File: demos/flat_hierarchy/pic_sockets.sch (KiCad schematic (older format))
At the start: 8 parts, among them P2 SUPP28, P3 SUPP40, U1 24Cxx, U5 PIC_18_PINS, U6 PIC_8_PINS

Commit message: Update demo files
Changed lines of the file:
@@
 EESchema Schematic File Version 2
-LIBS:power,device,transistors,conn,linear,regul,74xx,cmos4000,adc-dac,memory,xilinx,special,microcontrollers,dsp,microchip,analog_switches,motorola,texas,intel,audio,interface,digital-audio,philips,display,cypress,siliconi,contrib,valves
-EELAYER 23  0
+LIBS:power
+LIBS:device
+LIBS:transistors
+LIBS:conn
+LIBS:linear
+LIBS:regul
+LIBS:74xx
+LIBS:cmos4000
+LIBS:adc-dac
+LIBS:memory
+LIBS:xilinx
+LIBS:special
+LIBS:microcontrollers
+LIBS:dsp
+LIBS:microchip
+LIBS:analog_switches
+LIBS:motorola
+LIBS:texas
+LIBS:intel
+LIBS:audio
+LIBS:interface
+LIBS:digital-audio
+LIBS:philips
+LIBS:display
+LIBS:cypress
+LIBS:siliconi
+LIBS:opto
+LIBS:atmel
+LIBS:flat_hierarchy-cache
+EELAYER 24 0
 EELAYER END
-$Descr A4 11700 8267
+$Descr A4 11693 8268
+encoding utf-8
 Sheet 2 3
 Title "JDM - COM84 PIC Programmer with 13V DC/DC converter"
@@
 Comment4 ""
 $EndDescr
-Text GLabel 2350 1900 0    60   Input
+Text GLabel 2350 1900 0    60   Input ~ 0
 VPP-MCLR
-Text GLabel 2350 1700 0    60   Input
-CLOCK-RB6
-Text GLabel 2350 1500 0    60   Input
-DATA-RB7
-Text GLabel 2350 2150 0    60   Input
-VCC_PIC
-Text Label 2550 2150 0    60   ~
-VCC_PIC
-Text Label 2450 3150 0    60   ~
+Text GLabel 2350 1700 0    60   Input ~ 0
+CLOCK-RB6
+Text GLabel 2350 1500 0    60   Input ~ 0
+DATA-RB7
+Text GLabel 2350 2150 0    60   Input ~ 0
+VCC_PIC
+Text Label 2550 2150 0    60   ~ 0
+VCC_PIC
+Text Label 2450 3150 0    60   ~ 0
 VPP-MCLR
 Wire Wire Line
@@
 Wire Wire Line
 	4550 6900 4550 7000
-Text Label 3950 6900 0    60   ~
+Text Label 3950 6900 0    60   ~ 0
 VCC_PIC
 $Comp
@@
 U 1 1 4639BE2E
 P 4550 7400
-F 0 "#PWR01" H 4550 7400 30  0001 C C
-F 1 "GND" H 4550 7330 30  0001 C C
+F 0 "#PWR01" H 4550 7400 30  0001 C CNN
+F 1 "GND" H 4550 7330 30  0001 C CNN
+F 2 "" H 4550 7400 60  0001 C CNN
+F 3 "" H 4550 7400 60  0001 C CNN
 	1    4550 7400
 	1    0    0    -1
@@
 U 1 1 4639BE2C
 P 4550 7200
-F 0 "C8" H 4600 7300 50  0000 L C
-F 1 "100nF" H 4600 7100 50  0000 L C
+F 0 "C8" H 4600 7300 50  0000 L CNN
+F 1 "100nF" H 4600 7100 50  0000 L CNN
+F 2 "" H 4550 7200 60  0001 C CNN
+F 3 "" H 4550 7200 60  0001 C CNN
 	1    4550 7200
 	1    0    0    -1
 $EndComp
-Text Label 7650 5150 0    60   ~
-VCC_PIC
-Text Label 9900 4950 0    60   ~
-VCC_PIC
-Text Label 9650 2500 0    60   ~
+Text Label 7650 5150 0    60   ~ 0
+VCC_PIC
+Text Label 9900 4950 0    60   ~ 0
+VCC_PIC
+Text Label 9650 2500 0    60   ~ 0
 VCC_PIC
 $Comp
@@
 U 1 1 442A8794
 P 8450 5250
-F 0 "#PWR02" H 8450 5250 30  0001 C C
-F 1 "GND" H 8450 5180 30  0001 C C
+F 0 "#PWR02" H 8450 5250 30  0001 C CNN
+F 1 "GND" H 8450 5180 30  0001 C CNN
+F 2 "" H 8450 5250 60  0001 C CNN
+F 3 "" H 8450 5250 60  0001 C CNN
 	1    8450 5250
 	0    1    1    0
 $EndComp
-Text Label 4300 4850 0    60   ~
+Text Label 4300 4850 0    60   ~ 0
 VCC_PIC
 $Comp
@@
 U 1 1 443CCA5D
 P 8450 4850
-F 0 "#PWR03" H 8450 4850 30  0001 C C
-F 1 "GND" H 8450 4780 30  0001 C C
+F 0 "#PWR03" H 8450 4850 30  0001 C CNN
+F 1 "GND" H 8450 4780 30  0001 C CNN
+F 2 "" H 8450 4850 60  0001 C CNN
+F 3 "" H 8450 4850 60  0001 C CNN
 	1    8450 4850
 	0    1    1    0
@@
 U 1 1 443697C7
 P 9400 2600
-F 0 "#PWR04" H 9400 2600 30  0001 C C
-F 1 "GND" H 9400 2530 30  0001 C C
+F 0 "#PWR04" H 9400 2600 30  0001 C CNN
+F 1 "GND" H 9400 2530 30  0001 C CNN
+F 2 "" H 9400 2600 60  0001 C CNN
+F 3 "" H 9400 2600 60  0001 C CNN
 	1    9400 2600
 	0    -1   -1   0
@@
 U 1 1 443697C3
 P 8200 2400
-F 0 "#PWR05" H 8200 2400 30  0001 C C
-F 1 "GND" H 8200 2330 30  0001 C C
+F 0 "#PWR05" H 8200 2400 30  0001 C CNN
+F 1 "GND" H 8200 2330 30  0001 C CNN
+F 2 "" H 8200 2400 60  0001 C CNN
+F 3 "" H 8200 2400 60  0001 C CNN
 	1    8200 2400
 	0    1    1    0
 $EndComp
-Text Label 9550 1800 0    60   ~
-CLOCK-RB6
-Text Label 9550 1700 0    60   ~
-DATA-RB7
-Text Label 7550 1700 0    60   ~
+Text Label 9550 1800 0    60   ~ 0
+CLOCK-RB6
+Text Label 9550 1700 0    60   ~ 0
+DATA-RB7
+Text Label 7550 1700 0    60   ~ 0
 VPP-MCLR
 $Comp
@@
 U 1 1 4436967E
 P 8800 2350
-F 0 "P2" H 8850 3150 70  0000 C C
-F 1 "SUPP28" H 8800 1550 70  0000 C C
+F 0 "P2" H 8850 3150 70  0000 C CNN
+F 1 "SUPP28" H 8800 1550 70  0000 C CNN
+F 2 "" H 8800 2350 60  0001 C CNN
+F 3 "" H 8800 2350 60  0001 C CNN
 	1    8800 2350
 	1    0    0    -1
@@
 U 1 1 442AA147
 P 3700 7400
-F 0 "#PWR06" H 3700 7400 30  0001 C C
-F 1 "GND" H 3700 7330 30  0001 C C
+F 0 "#PWR06" H 3700 7400 30  0001 C CNN
+F 1 "GND" H 3700 7330 30  0001 C CNN
+F 2 "" H 3700 7400 60  0001 C CNN
+F 3 "" H 3700 7400 60  0001 C CNN
 	1    3700 7400
 	1    0    0    -1
@@
 U 1 1 442AA145
 P 3700 7200
-F 0 "C7" H 3750 7300 50  0000 L C
-F 1 "100nF" H 3750 7100 50  0000 L C
+F 0 "C7" H 3750 7300 50  0000 L CNN
+F 1 "100nF" H 3750 7100 50  0000 L CNN
+F 2 "" H 3700 7200 60  0001 C CNN
+F 3 "" H 3700 7200 60  0001 C CNN
 	1    3700 7200
 	1    0    0    -1
@@
 U 1 1 442AA138
 P 2700 7400
-F 0 "#PWR07" H 2700 7400 30  0001 C C
-F 1 "GND" H 2700 7330 30  0001 C C
+F 0 "#PWR07" H 2700 7400 30  0001 C CNN
+F 1 "GND" H 2700 7330 30  0001 C CNN
+F 2 "" H 2700 7400 60  0001 C CNN
+F 3 "" H 2700 7400 60  0001 C CNN
 	1    2700 7400
 	1    0    0    -1
@@
 U 1 1 442AA134
 P 2700 7000
-F 0 "#PWR08" H 2700 7100 30  0001 C C
-F 1 "VCC" H 2700 7100 30  0000 C C
+F 0 "#PWR08" H 2700 7100 30  0001 C CNN
+F 1 "VCC" H 2700 7100 30  0000 C CNN
+F 2 "" H 2700 7000 60  0001 C CNN
+F 3 "" H 2700 7000 60  0001 C CNN
 	1    2700 7000
 	1    0    0    -1
@@
 U 1 1 442AA12B
 P 2700 7200
-F 0 "C6" H 2750 7300 50  0000 L C
-F 1 "100nF" H 2750 7100 50  0000 L C
+F 0 "C6" H 2750 7300 50  0000 L CNN
+F 1 "100nF" H 2750 7100 50  0000 L CNN
+F 2 "" H 2700 7200 60  0001 C CNN
+F 3 "" H 2700 7200 60  0001 C CNN
 	1    2700 7200
 	1    0    0    -1
@@
 U 1 1 442A896A
 P 9650 5050
-F 0 "#PWR09" H 9650 5050 30  0001 C C
-F 1 "GND" H 9650 4980 30  0001 C C
+F 0 "#PWR09" H 9650 5050 30  0001 C CNN
+F 1 "GND" H 9650 4980 30  0001 C CNN
+F 2 "" H 9650 5050 60  0001 C CNN
+F 3 "" H 9650 5050 60  0001 C CNN
 	1    9650 5050
 	0    -1   -1   0
@@
 U 1 1 442A88ED
 P 9050 5100
-F 0 "P3" H 9100 6200 70  0000 C C
-F 1 "SUPP40" H 8900 4000 70  0000 C C
+F 0 "P3" H 9100 6200 70  0000 C CNN
+F 1 "SUPP40" H 8900 4000 70  0000 C CNN
+F 2 "" H 9050 5100 60  0001 C CNN
+F 3 "" H 9050 5100 60  0001 C CNN
 	1    9050 5100
 	1    0    0    -1
@@
 U 1 1 442A8838
 P 2950 1250
-F 0 "#PWR010" H 2950 1250 30  0001 C C
-F 1 "GND" H 2950 1180 30  0001 C C
+F 0 "#PWR010" H 2950 1250 30  0001 C CNN
+F 1 "GND" H 2950 1180 30  0001 C CNN
+F 2 "" H 2950 1250 60  0001 C CNN
+F 3 "" H 2950 1250 60  0001 C CNN
 	1    2950 1250
 	1    0    0    -1
 $EndComp
-Text Label 4700 1400 0    60   ~
-DATA-RB7
-Text Label 4700 1300 0    60   ~
+Text Label 4700 1400 0    60   ~ 0
+DATA-RB7
+Text Label 4700 1300 0    60   ~ 0
 CLOCK-RB6
 $Comp
@@
 U 1 1 442A87F7
 P 3850 1200
-F 0 "U1" H 4000 1550 60  0000 C C
-F 1 "24Cxx" H 4050 850 60  0000 C C
+F 0 "U1" H 4000 1550 60  0000 C CNN
+F 1 "24Cxx" H 4050 850 60  0000 C CNN
+F 2 "" H 3850 1200 60  0001 C CNN
+F 3 "" H 3850 1200 60  0001 C CNN
 	1    3850 1200
 	1    0    0    -1
 $EndComp
-Text Label 9800 4250 0    60   ~
-CLOCK-RB6
-Text Label 9800 4150 0    60   ~
-DATA-RB7
-Text Label 7800 4150 0    60   ~
+Text Label 9800 4250 0    60   ~ 0
+CLOCK-RB6
+Text Label 9800 4150 0    60   ~ 0
+DATA-RB7
+Text Label 7800 4150 0    60   ~ 0
 VPP-MCLR
 NoConn ~ 2500 4400
@@
 U 1 1 442A81A7
 P 3300 4850
-F 0 "U5" H 3600 5650 60  0000 C C
-F 1 "PIC_18_PINS" H 3750 4050 60  0000 C C
+F 0 "U5" H 3600 5650 60  0000 C CNN
+F 1 "PIC_18_PINS" H 3750 4050 60  0000 C CNN
+F 2 "" H 3300 4850 60  0001 C CNN
+F 3 "" H 3300 4850 60  0001 C CNN
 	1    3300 4850
 	1    0    0    -1
@@
 NoConn ~ 3100 2850
 NoConn ~ 3100 2450
-Text Label 4200 5150 0    60   ~
-CLOCK-RB6
-Text Label 4200 5000 0    60   ~
-DATA-RB7
-Text Label 1850 4700 0    60   ~
+Text Label 4200 5150 0    60   ~ 0
+CLOCK-RB6
+Text Label 4200 5000 0    60   ~ 0
+DATA-RB7
+Text Label 1850 4700 0    60   ~ 0
 VPP-MCLR
-Text Label 4700 2850 0    60   ~
-CLOCK-RB6
-Text Label 4700 2450 0    60   ~
+Text Label 4700 2850 0    60   ~ 0
+CLOCK-RB6
+Text Label 4700 2450 0    60   ~ 0
 DATA-RB7
 $Comp
@@
 U 1 1 442A820F
 P 2300 4900
-F 0 "#PWR011" H 2300 4900 30  0001 C C
-F 1 "GND" H 2300 4830 30  0001 C C
+F 0 "#PWR011" H 2300 4900 30  0001 C CNN
+F 1 "GND" H 2300 4830 30  0001 C CNN
+F 2 "" H 2300 4900 60  0001 C CNN
+F 3 "" H 2300 4900 60  0001 C CNN
 	1    2300 4900
 	1    0    0    -1
@@
 U 1 1 442A8205
 P 4550 2150
-F 0 "#PWR012" H 4550 2150 30  0001 C C
-F 1 "GND" H 4550 2080 30  0001 C C
+F 0 "#PWR012" H 4550 2150 30  0001 C CNN
+F 1 "GND" H 4550 2080 30  0001 C CNN
+F 2 "" H 4550 2150 60  0001 C CNN
+F 3 "" H 4550 2150 60  0001 C CNN
 	1    4550 2150
 	0    -1   -1   0
@@
 U 1 1 442A81A5
 P 3850 2650
-F 0 "U6" H 3800 3350 60  0000 C C
-F 1 "PIC_8_PINS" H 3850 1950 60  0000 C C
+F 0 "U6" H 3800 3350 60  0000 C CNN
+F 1 "PIC_8_PINS" H 3850 1950 60  0000 C CNN
+F 2 "" H 3850 2650 60  0001 C CNN
+F 3 "" H 3850 2650 60  0001 C CNN
 	1    3850 2650
 	1    0    0    -1
 $EndComp
+$Comp
+L VCC #PWR013
+U 1 1 53B84749
+P 3850 700
+F 0 "#PWR013" H 3850 800 30  0001 C CNN
+F 1 "VCC" H 3850 800 30  0000 C CNN
+F 2 "" H 3850 700 60  0001 C CNN
+F 3 "" H 3850 700 60  0001 C CNN
+	1    3850 700
+	1    0    0    -1
+$EndComp
+$Comp
+L GND #PWR014
+U 1 1 53B847AC
+P 3850 1700
+F 0 "#PWR014" H 3850 1700 30  0001 C CNN
+F 1 "GND" H 3850 1630 30  0001 C CNN
+F 2 "" H 3850 1700 60  0001 C CNN
+F 3 "" H 3850 1700 60  0001 C CNN
+	1    3850 1700
+	1    0    0    -1
+$EndComp

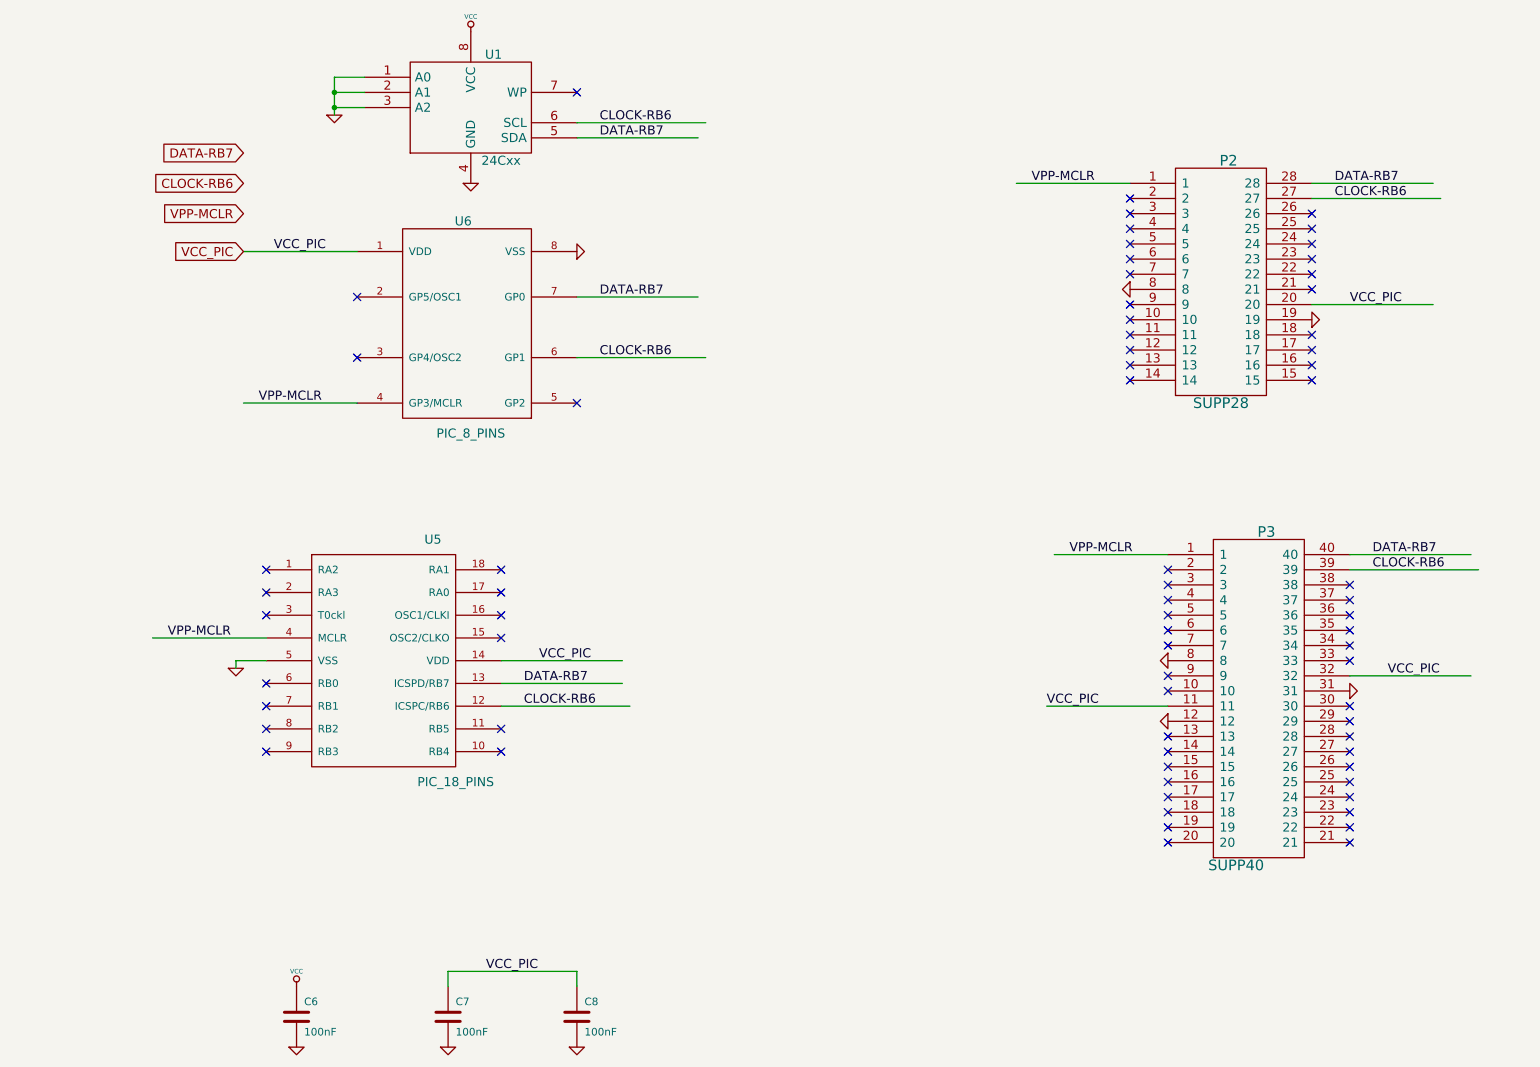
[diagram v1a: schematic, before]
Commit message: demos/ schematic tidying
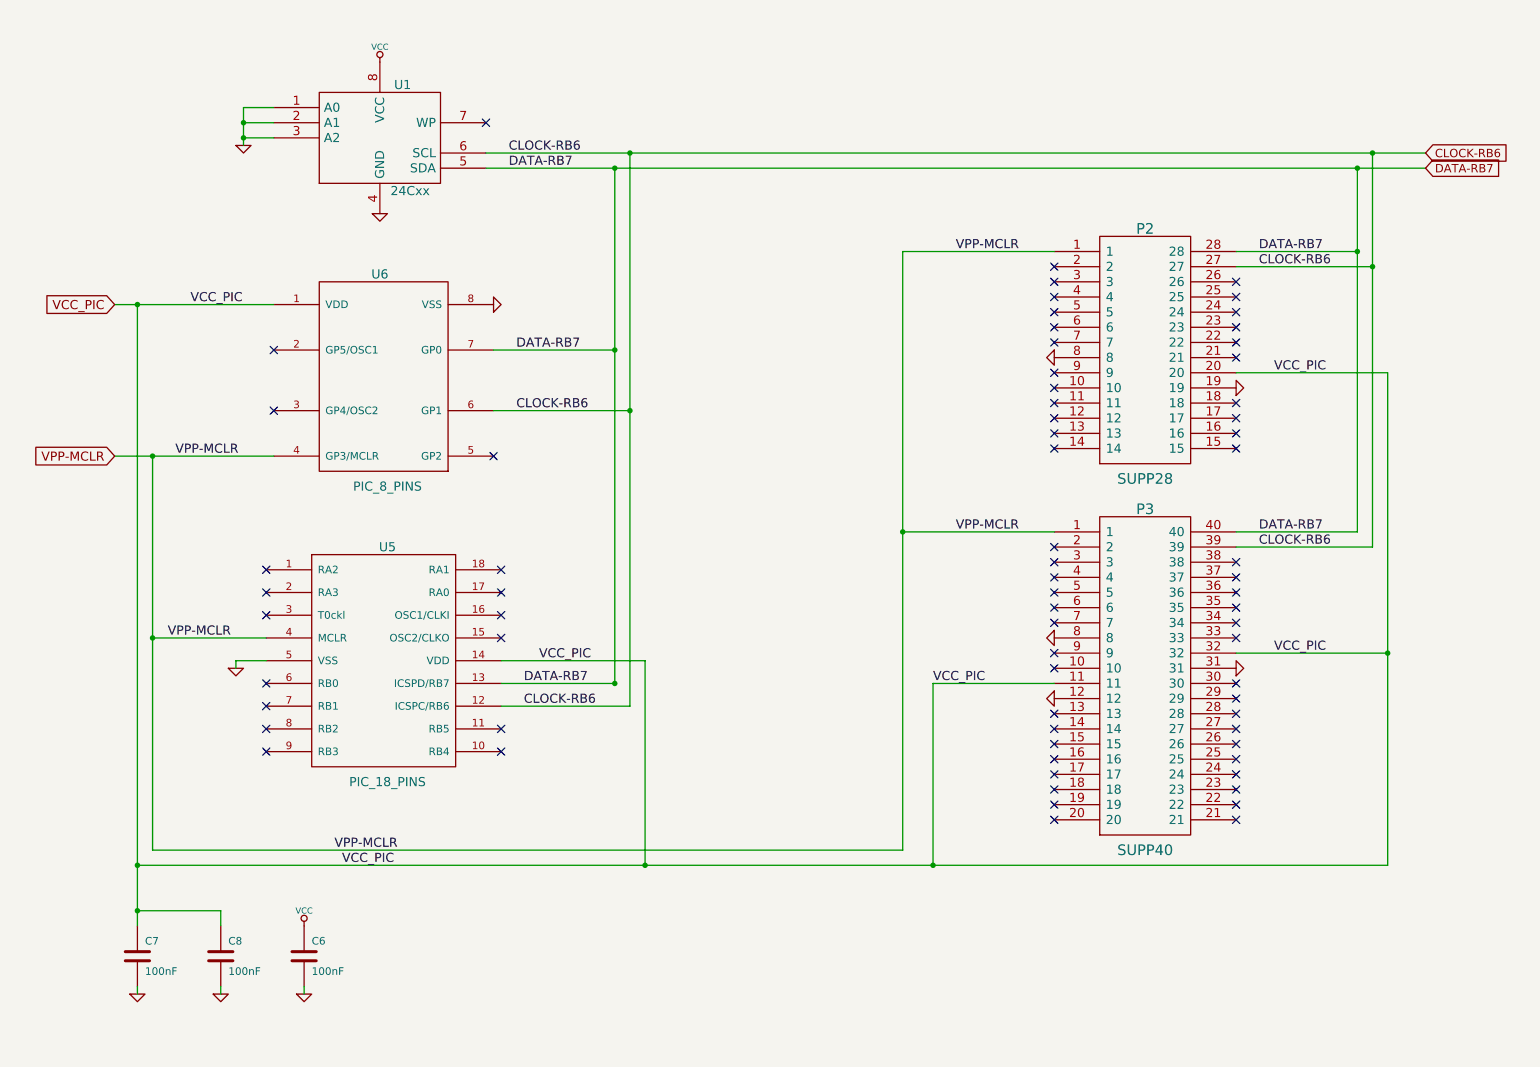
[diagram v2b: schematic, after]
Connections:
- wire segments 28 -> 42
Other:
- moved on the sheet: C6, C7, C8, P2, P3, U1, U6

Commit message: polygons in footprint body: fix incorrect calculation of polygons with clearance or outline thickness (fix bug #1511366) Clean demos
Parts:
- C6, C7, C8: footprint (none) -> Discret:C1-1
- P2: footprint (none) -> Sockets_DIP:DIP-28__300_ELL
- P3: footprint (none) -> Sockets_DIP:DIP-40__600_ELL
- U1, U6: footprint (none) -> Sockets_DIP:DIP-8__300_ELL
- U5: footprint (none) -> Sockets_DIP:DIP-18__300_ELL
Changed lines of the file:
@@
 F 0 "C8" H 2250 6900 50  0000 L CNN
 F 1 "100nF" H 2250 6700 50  0000 L CNN
-F 2 "" H 2200 6800 60  0001 C CNN
+F 2 "Discret:C1-1" H 2200 6800 60  0001 C CNN
 F 3 "" H 2200 6800 60  0001 C CNN
 	1    2200 6800
@@
 F 0 "P2" H 8300 3600 70  0000 C CNN
 F 1 "SUPP28" H 8300 1950 70  0000 C CNN
-F 2 "" H 8300 2800 60  0001 C CNN
+F 2 "Sockets_DIP:DIP-28__300_ELL" H 8300 2800 60  0001 C CNN
 F 3 "" H 8300 2800 60  0001 C CNN
 	1    8300 2800
@@
 F 0 "C7" H 1700 6900 50  0000 L CNN
 F 1 "100nF" H 1700 6700 50  0000 L CNN
-F 2 "" H 1650 6800 60  0001 C CNN
+F 2 "Discret:C1-1" H 1650 6800 60  0001 C CNN
 F 3 "" H 1650 6800 60  0001 C CNN
 	1    1650 6800
@@
 F 0 "C6" H 2800 6900 50  0000 L CNN
 F 1 "100nF" H 2800 6700 50  0000 L CNN
-F 2 "" H 2750 6800 60  0001 C CNN
+F 2 "Discret:C1-1" H 2750 6800 60  0001 C CNN
 F 3 "" H 2750 6800 60  0001 C CNN
 	1    2750 6800
@@
 F 0 "P3" H 8300 6050 70  0000 C CNN
 F 1 "SUPP40" H 8300 3800 70  0000 C CNN
-F 2 "" H 8300 4950 60  0001 C CNN
+F 2 "Sockets_DIP:DIP-40__600_ELL" H 8300 4950 60  0001 C CNN
 F 3 "" H 8300 4950 60  0001 C CNN
 	1    8300 4950
@@
 F 0 "U1" H 3400 1750 60  0000 C CNN
 F 1 "24Cxx" H 3450 1050 60  0000 C CNN
-F 2 "" H 3250 1400 60  0001 C CNN
+F 2 "Sockets_DIP:DIP-8__300_ELL" H 3250 1400 60  0001 C CNN
 F 3 "" H 3250 1400 60  0001 C CNN
 	1    3250 1400
@@
 F 0 "U5" H 3300 5600 60  0000 C CNN
 F 1 "PIC_18_PINS" H 3300 4050 60  0000 C CNN
-F 2 "" H 3300 4850 60  0001 C CNN
+F 2 "Sockets_DIP:DIP-18__300_ELL" H 3300 4850 60  0001 C CNN
 F 3 "" H 3300 4850 60  0001 C CNN
 	1    3300 4850
@@
 F 0 "U6" H 3250 3700 60  0000 C CNN
 F 1 "PIC_8_PINS" H 3300 2300 60  0000 C CNN
-F 2 "" H 3300 3000 60  0001 C CNN
+F 2 "Sockets_DIP:DIP-8__300_ELL" H 3300 3000 60  0001 C CNN
 F 3 "" H 3300 3000 60  0001 C CNN
 	1    3300 3000
